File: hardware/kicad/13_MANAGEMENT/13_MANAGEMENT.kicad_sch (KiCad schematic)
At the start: 1 part

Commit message: M3.7: restore native Slice A passive instances
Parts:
- added C_MGMT_VREG_AVDD, C_MGMT_VREG_IN, C_MGMT_VREG_OUT: 4.7uF, symbol RetroSBC-management:C_LOCAL
- added L_MGMT_CORE: 3.3uH, symbol RetroSBC-management:L_LOCAL
- added R_MGMT_VREG_AVDD: 33R, symbol RetroSBC-management:R_LOCAL
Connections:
- net GND: now also C_MGMT_VREG_AVDD.2, C_MGMT_VREG_IN.2, C_MGMT_VREG_OUT.2
- net MGMT_1V1: now also C_MGMT_VREG_OUT.1, L_MGMT_CORE.2
- net MGMT_3V3: now also C_MGMT_VREG_IN.1, R_MGMT_VREG_AVDD.1
- net VREG_AVDD: now also C_MGMT_VREG_AVDD.1, R_MGMT_VREG_AVDD.2
- new net VREG_LX: L_MGMT_CORE.1
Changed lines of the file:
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@@
     ))
   )
+  (symbol (lib_id "RetroSBC-management:L_LOCAL") (at 149.86 80 0) (unit 1)
+    (exclude_from_sim no) (in_bom yes) (on_board yes)
+    (property "Reference" "L_MGMT_CORE" (at 149.86 77.46 0) (effects (font (size 1.27 1.27))))
+    (property "Value" "3.3uH" (at 149.86 82.54 0) (effects (font (size 1.27 1.27))))
+    (property "Footprint" "" (at 149.86 80 0) (effects (font (size 1.27 1.27)) hide))
+    (property "Datasheet" "" (at 149.86 80 0) (effects (font (size 1.27 1.27)) hide))
+    (property "Description" "RetroSBC local passive" (at 149.86 80 0) (effects (font (size 1.27 1.27)) hide))
+    (pin "1")
+    (pin "2")
+    (instances (project "RetroSBC-13-MANAGEMENT" (path "/7a5d3d51-9e2f-4d31-b7cb-9fbd10b8c301/21111111-1111-4111-8111-222222222222" (reference "L_MGMT_CORE") (unit 1))))
+  )
+  (label "VREG_LX" (at 144.78 80 0) (effects (font (size 1.27 1.27)) (justify right bottom)))
+  (label "MGMT_1V1" (at 154.94 80 180) (effects (font (size 1.27 1.27)) (justify right bottom)))
+  (symbol (lib_id "RetroSBC-management:C_LOCAL") (at 149.86 90 0) (unit 1)
+    (exclude_from_sim no) (in_bom yes) (on_board yes)
+    (property "Reference" "C_MGMT_VREG_IN" (at 149.86 87.46 0) (effects (font (size 1.27 1.27))))
+    (property "Value" "4.7uF" (at 149.86 92.54 0) (effects (font (size 1.27 1.27))))
+    (property "Footprint" "" (at 149.86 90 0) (effects (font (size 1.27 1.27)) hide))
+    (property "Datasheet" "" (at 149.86 90 0) (effects (font (size 1.27 1.27)) hide))
+    (property "Description" "RetroSBC local passive" (at 149.86 90 0) (effects (font (size 1.27 1.27)) hide))
+    (pin "1")
+    (pin "2")
+    (instances (project "RetroSBC-13-MANAGEMENT" (path "/7a5d3d51-9e2f-4d31-b7cb-9fbd10b8c301/31111111-1111-4111-8111-333333333333" (reference "C_MGMT_VREG_IN") (unit 1))))
+  )
+  (label "MGMT_3V3" (at 144.78 90 0) (effects (font (size 1.27 1.27)) (justify right bottom)))
+  (label "GND" (at 154.94 90 180) (effects (font (size 1.27 1.27)) (justify right bottom)))
+  (symbol (lib_id "RetroSBC-management:C_LOCAL") (at 149.86 100 0) (unit 1)
+    (exclude_from_sim no) (in_bom yes) (on_board yes)
+    (property "Reference" "C_MGMT_VREG_OUT" (at 149.86 97.46 0) (effects (font (size 1.27 1.27))))
+    (property "Value" "4.7uF" (at 149.86 102.54 0) (effects (font (size 1.27 1.27))))
+    (property "Footprint" "" (at 149.86 100 0) (effects (font (size 1.27 1.27)) hide))
+    (property "Datasheet" "" (at 149.86 100 0) (effects (font (size 1.27 1.27)) hide))
+    (property "Description" "RetroSBC local passive" (at 149.86 100 0) (effects (font (size 1.27 1.27)) hide))
+    (pin "1")
+    (pin "2")
+    (instances (project "RetroSBC-13-MANAGEMENT" (path "/7a5d3d51-9e2f-4d31-b7cb-9fbd10b8c301/41111111-1111-4111-8111-444444444444" (reference "C_MGMT_VREG_OUT") (unit 1))))
+  )
+  (label "MGMT_1V1" (at 144.78 100 0) (effects (font (size 1.27 1.27)) (justify right bottom)))
+  (label "GND" (at 154.94 100 180) (effects (font (size 1.27 1.27)) (justify right bottom)))
+  (symbol (lib_id "RetroSBC-management:R_LOCAL") (at 149.86 110 0) (unit 1)
+    (exclude_from_sim no) (in_bom yes) (on_board yes)
+    (property "Reference" "R_MGMT_VREG_AVDD" (at 149.86 107.46 0) (effects (font (size 1.27 1.27))))
+    (property "Value" "33R" (at 149.86 112.54 0) (effects (font (size 1.27 1.27))))
+    (property "Footprint" "" (at 149.86 110 0) (effects (font (size 1.27 1.27)) hide))
+    (property "Datasheet" "" (at 149.86 110 0) (effects (font (size 1.27 1.27)) hide))
+    (property "Description" "RetroSBC local passive" (at 149.86 110 0) (effects (font (size 1.27 1.27)) hide))
+    (pin "1")
+    (pin "2")
+    (instances (project "RetroSBC-13-MANAGEMENT" (path "/7a5d3d51-9e2f-4d31-b7cb-9fbd10b8c301/51111111-1111-4111-8111-555555555555" (reference "R_MGMT_VREG_AVDD") (unit 1))))
+  )
+  (label "MGMT_3V3" (at 144.78 110 0) (effects (font (size 1.27 1.27)) (justify right bottom)))
+  (label "VREG_AVDD" (at 154.94 110 180) (effects (font (size 1.27 1.27)) (justify right bottom)))
+  (symbol (lib_id "RetroSBC-management:C_LOCAL") (at 149.86 120 0) (unit 1)
+    (exclude_from_sim no) (in_bom yes) (on_board yes)
+    (property "Reference" "C_MGMT_VREG_AVDD" (at 149.86 117.46 0) (effects (font (size 1.27 1.27))))
+    (property "Value" "4.7uF" (at 149.86 122.54 0) (effects (font (size 1.27 1.27))))
+    (property "Footprint" "" (at 149.86 120 0) (effects (font (size 1.27 1.27)) hide))
+    (property "Datasheet" "" (at 149.86 120 0) (effects (font (size 1.27 1.27)) hide))
+    (property "Description" "RetroSBC local passive" (at 149.86 120 0) (effects (font (size 1.27 1.27)) hide))
+    (pin "1")
+    (pin "2")
+    (instances (project "RetroSBC-13-MANAGEMENT" (path "/7a5d3d51-9e2f-4d31-b7cb-9fbd10b8c301/61111111-1111-4111-8111-666666666666" (reference "C_MGMT_VREG_AVDD") (unit 1))))
+  )
+  (label "VREG_AVDD" (at 144.78 120 0) (effects (font (size 1.27 1.27)) (justify right bottom)))
+  (label "GND" (at 154.94 120 180) (effects (font (size 1.27 1.27)) (justify right bottom)))
+  (label "MGMT_3V3" (at 69.52000000000001 113.97 0)
+    (effects (font (size 1.27 1.27)) (justify left bottom))
+)
+  (label "MGMT_1V1" (at 69.52000000000001 101.27 0)
+    (effects (font (size 1.27 1.27)) (justify left bottom))
+)
+  (label "MGMT_3V3" (at 69.52000000000001 88.57 0)
+    (effects (font (size 1.27 1.27)) (justify left bottom))
+)
+  (label "MGMT_3V3" (at 87.03999999999999 74.6 90)
+    (effects (font (size 1.27 1.27)) (justify left bottom))
+)
+  (label "MGMT_3V3" (at 97.19 74.6 90)
+    (effects (font (size 1.27 1.27)) (justify left bottom))
+)
+  (label "MGMT_1V1" (at 103.28 74.6 90)
+    (effects (font (size 1.27 1.27)) (justify left bottom))
+)
+  (label "MGMT_3V3" (at 130.48 75.87 180)
+    (effects (font (size 1.27 1.27)) (justify left bottom))
+)
+  (label "MGMT_3V3" (at 130.48 98.73 180)
+    (effects (font (size 1.27 1.27)) (justify left bottom))
+)
+  (label "MGMT_1V1" (at 130.48 101.27 180)
+    (effects (font (size 1.27 1.27)) (justify left bottom))
+)
+  (label "MGMT_3V3" (at 130.48 121.59 180)
+    (effects (font (size 1.27 1.27)) (justify left bottom))
+)
+  (label "MGMT_3V3" (at 130.48 124.13 180)
+    (effects (font (size 1.27 1.27)) (justify left bottom))
+)
+  (label "MGMT_3V3" (at 104.84 125.4 270)
+    (effects (font (size 1.27 1.27)) (justify left bottom))
+)
+  (label "MGMT_3V3" (at 102.81 125.4 270)
+    (effects (font (size 1.27 1.27)) (justify left bottom))
+)
+  (label "MGMT_3V3" (at 88.60000000000001 125.4 270)
+    (effects (font (size 1.27 1.27)) (justify left bottom))
+)
   (label "VREG_AVDD" (at 119.05 69.52 90)
     (effects (font (size 1.27 1.27)) (justify left bottom))

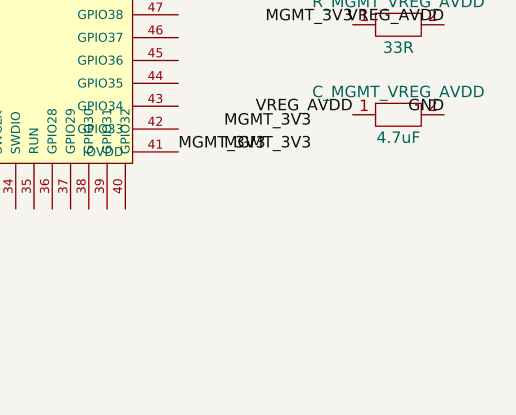
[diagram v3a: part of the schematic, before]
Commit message: M3.7: materialize locked management bulk and rail decoupling
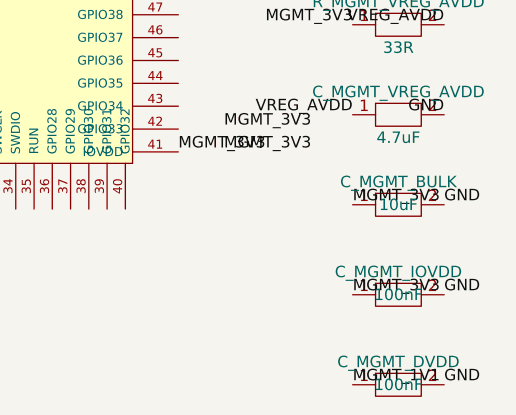
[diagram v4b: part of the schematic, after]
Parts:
- added C_MGMT_BULK: 10uF, symbol RetroSBC-management:C_LOCAL
- added C_MGMT_DVDD, C_MGMT_IOVDD: 100nF, symbol RetroSBC-management:C_LOCAL
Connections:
- net GND: now also C_MGMT_BULK.2, C_MGMT_DVDD.2, C_MGMT_IOVDD.2
- net MGMT_1V1: now also C_MGMT_DVDD.1
- net MGMT_3V3: now also C_MGMT_BULK.1, C_MGMT_IOVDD.1
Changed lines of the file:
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@@
+    (effects (font (size 1.27 1.27)) (justify left bottom))
+)
+  (symbol (lib_id "RetroSBC-management:C_LOCAL") (at 149.86 130 0) (unit 1)
+    (exclude_from_sim no) (in_bom yes) (on_board yes)
+    (property "Reference" "C_MGMT_BULK" (at 149.86 127.46 0) (effects (font (size 1.27 1.27))))
+    (property "Value" "10uF" (at 149.86 130 0) (effects (font (size 1.27 1.27))))
+    (property "Footprint" "" (at 149.86 130 0) (effects (font (size 1.27 1.27)) hide))
+    (property "Datasheet" "" (at 149.86 130 0) (effects (font (size 1.27 1.27)) hide))
+    (property "Description" "RetroSBC local passive" (at 149.86 130 0) (effects (font (size 1.27 1.27)) hide))
+    (pin "1")
+    (pin "2")
+    (instances (project "RetroSBC-13-MANAGEMENT"
+      (path "/7a5d3d51-9e2f-4d31-b7cb-9fbd10b8c301/c0000101-6666-4666-8666-000000000101" (reference "C_MGMT_BULK") (unit 1))
+    ))
+  )
+  (label "MGMT_3V3" (at 144.78 130 0)
+    (effects (font (size 1.27 1.27)) (justify left bottom))
+)
+  (label "GND" (at 154.94 130 180)
+    (effects (font (size 1.27 1.27)) (justify left bottom))
+)
+  (symbol (lib_id "RetroSBC-management:C_LOCAL") (at 149.86 140 0) (unit 1)
+    (exclude_from_sim no) (in_bom yes) (on_board yes)
+    (property "Reference" "C_MGMT_IOVDD" (at 149.86 137.46 0) (effects (font (size 1.27 1.27))))
+    (property "Value" "100nF" (at 149.86 140 0) (effects (font (size 1.27 1.27))))
+    (property "Footprint" "" (at 149.86 140 0) (effects (font (size 1.27 1.27)) hide))
+    (property "Datasheet" "" (at 149.86 140 0) (effects (font (size 1.27 1.27)) hide))
+    (property "Description" "RetroSBC local passive" (at 149.86 140 0) (effects (font (size 1.27 1.27)) hide))
+    (pin "1")
+    (pin "2")
+    (instances (project "RetroSBC-13-MANAGEMENT"
+      (path "/7a5d3d51-9e2f-4d31-b7cb-9fbd10b8c301/c0000102-6666-4666-8666-000000000102" (reference "C_MGMT_IOVDD") (unit 1))
+    ))
+  )
+  (label "MGMT_3V3" (at 144.78 140 0)
+    (effects (font (size 1.27 1.27)) (justify left bottom))
+)
+  (label "GND" (at 154.94 140 180)
+    (effects (font (size 1.27 1.27)) (justify left bottom))
+)
+  (symbol (lib_id "RetroSBC-management:C_LOCAL") (at 149.86 150 0) (unit 1)
+    (exclude_from_sim no) (in_bom yes) (on_board yes)
+    (property "Reference" "C_MGMT_DVDD" (at 149.86 147.46 0) (effects (font (size 1.27 1.27))))
+    (property "Value" "100nF" (at 149.86 150 0) (effects (font (size 1.27 1.27))))
+    (property "Footprint" "" (at 149.86 150 0) (effects (font (size 1.27 1.27)) hide))
+    (property "Datasheet" "" (at 149.86 150 0) (effects (font (size 1.27 1.27)) hide))
+    (property "Description" "RetroSBC local passive" (at 149.86 150 0) (effects (font (size 1.27 1.27)) hide))
+    (pin "1")
+    (pin "2")
+    (instances (project "RetroSBC-13-MANAGEMENT"
+      (path "/7a5d3d51-9e2f-4d31-b7cb-9fbd10b8c301/c0000103-6666-4666-8666-000000000103" (reference "C_MGMT_DVDD") (unit 1))
+    ))
+  )
+  (label "MGMT_1V1" (at 144.78 150 0)
+    (effects (font (size 1.27 1.27)) (justify left bottom))
+)
+  (label "GND" (at 154.94 150 180)
     (effects (font (size 1.27 1.27)) (justify left bottom))
 )

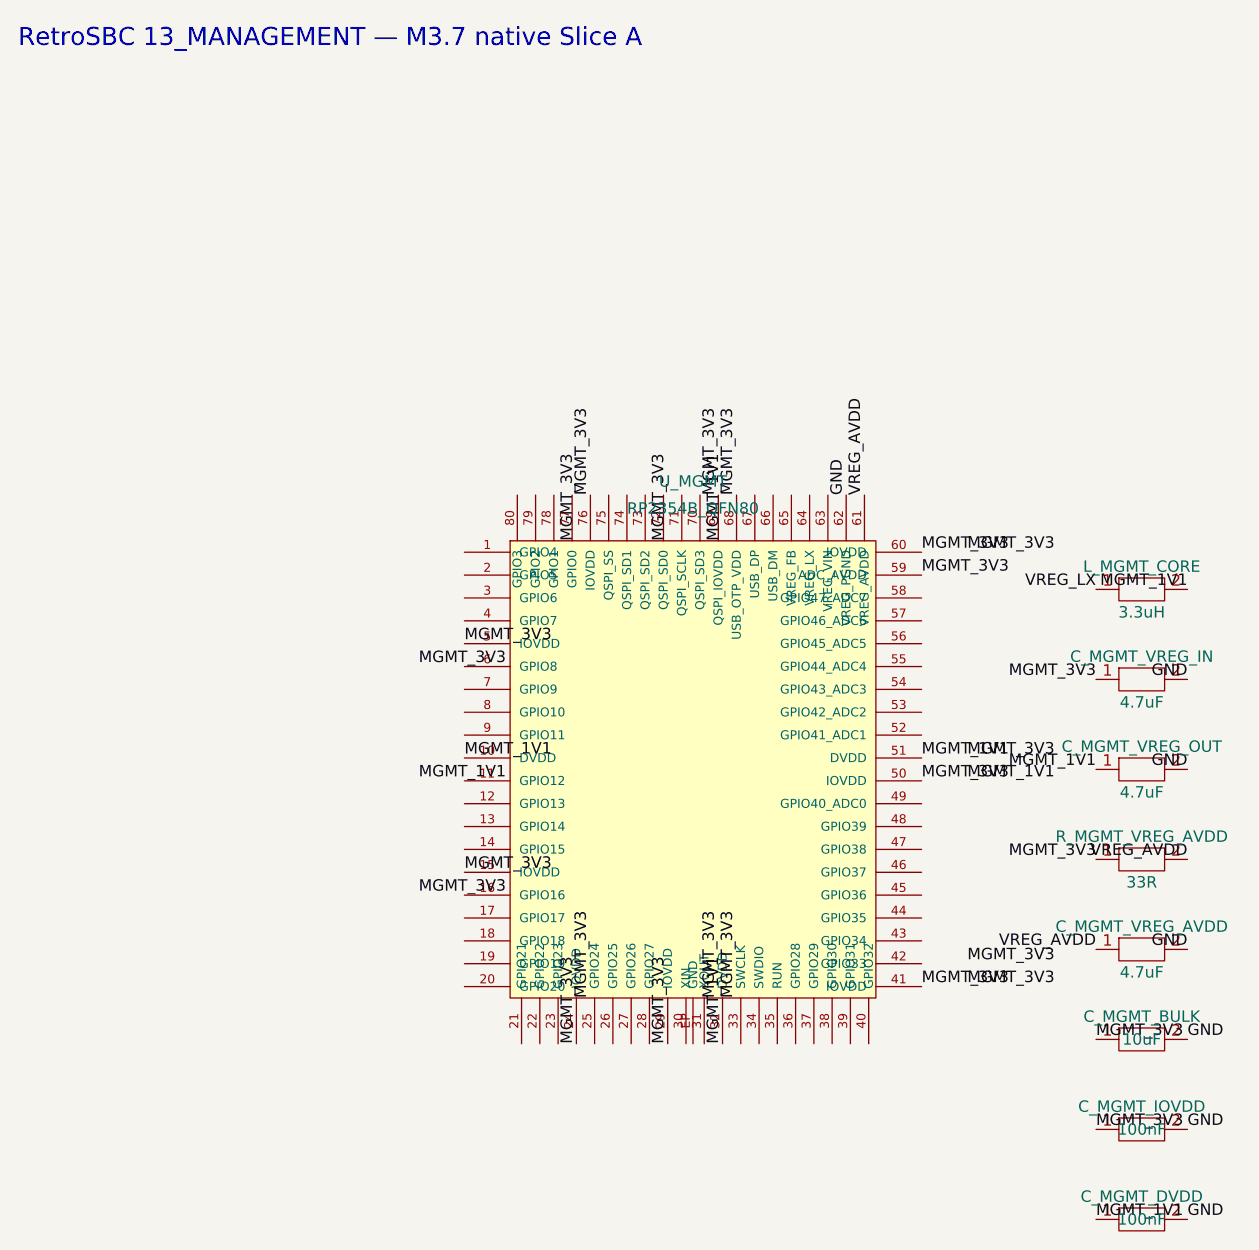
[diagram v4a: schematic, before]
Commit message: M3.7: remove stale Slice B labels and restore regulator endpoint nets
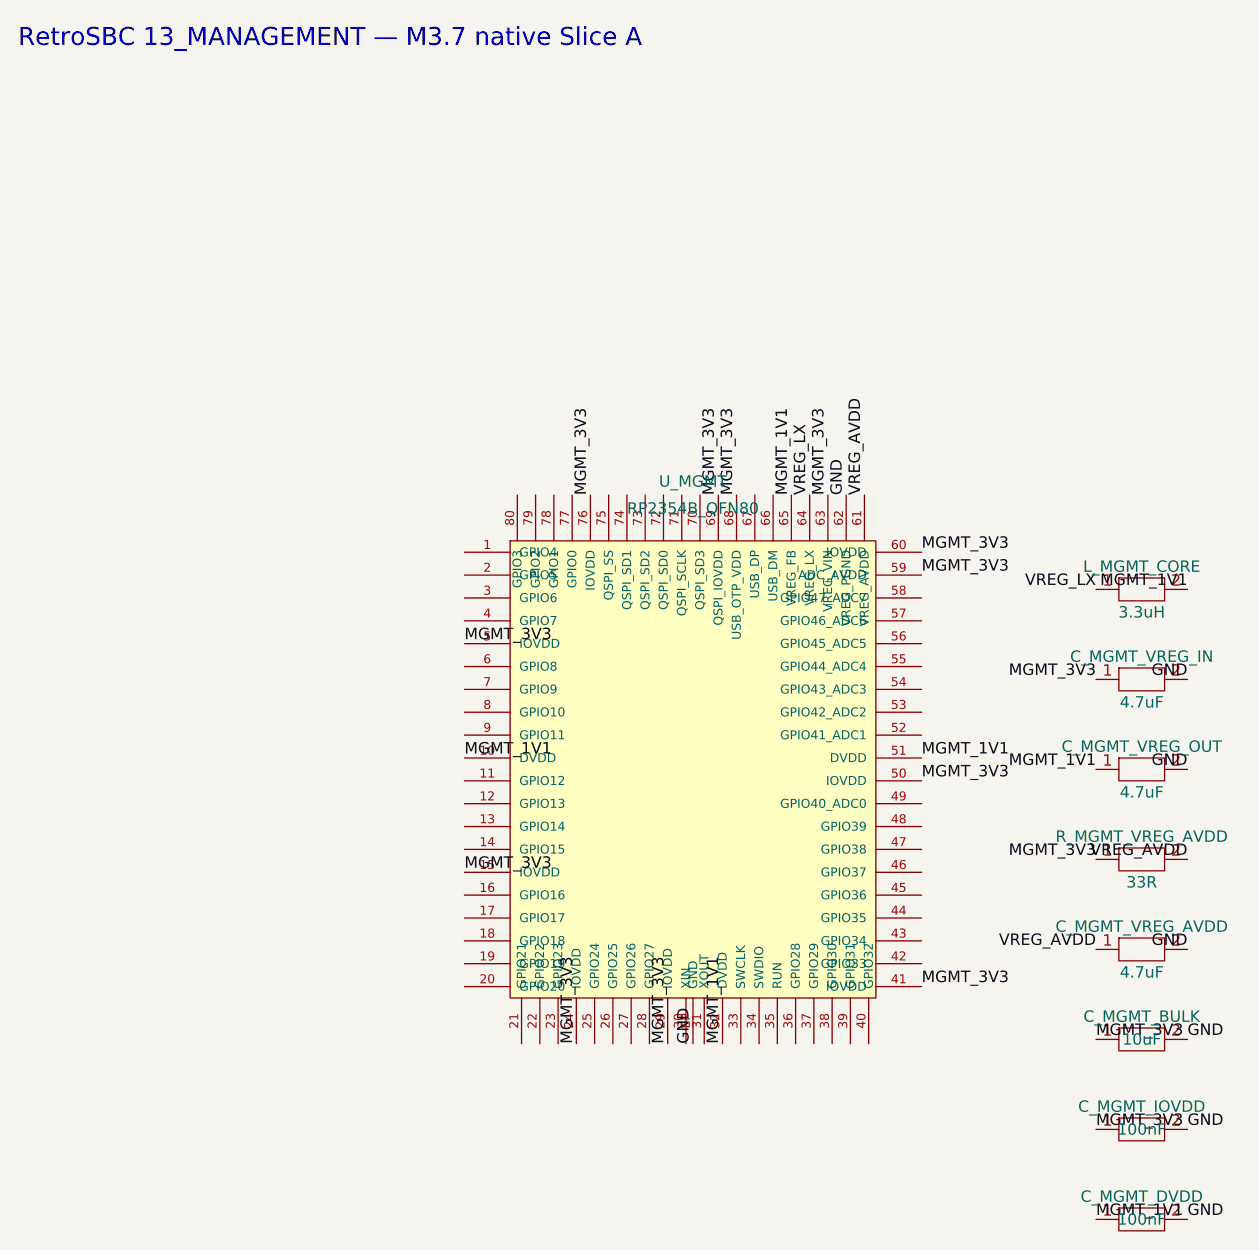
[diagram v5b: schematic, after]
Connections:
- net GND: now also U_MGMT.EP (GND)
- net MGMT_1V1: now also U_MGMT.65 (VREG_FB)
- net MGMT_3V3: now also U_MGMT.63 (VREG_VIN)
- net VREG_LX: now also U_MGMT.64 (VREG_LX)
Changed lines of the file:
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@@
   (label "VREG_AVDD" (at 144.78 120 0) (effects (font (size 1.27 1.27)) (justify right bottom)))
   (label "GND" (at 154.94 120 180) (effects (font (size 1.27 1.27)) (justify right bottom)))
-  (label "MGMT_3V3" (at 69.52000000000001 113.97 0)
-    (effects (font (size 1.27 1.27)) (justify left bottom))
-)
-  (label "MGMT_1V1" (at 69.52000000000001 101.27 0)
-    (effects (font (size 1.27 1.27)) (justify left bottom))
-)
-  (label "MGMT_3V3" (at 69.52000000000001 88.57 0)
-    (effects (font (size 1.27 1.27)) (justify left bottom))
-)
-  (label "MGMT_3V3" (at 87.03999999999999 74.6 90)
-    (effects (font (size 1.27 1.27)) (justify left bottom))
-)
-  (label "MGMT_3V3" (at 97.19 74.6 90)
-    (effects (font (size 1.27 1.27)) (justify left bottom))
-)
-  (label "MGMT_1V1" (at 103.28 74.6 90)
-    (effects (font (size 1.27 1.27)) (justify left bottom))
-)
-  (label "MGMT_3V3" (at 130.48 75.87 180)
-    (effects (font (size 1.27 1.27)) (justify left bottom))
-)
-  (label "MGMT_3V3" (at 130.48 98.73 180)
-    (effects (font (size 1.27 1.27)) (justify left bottom))
-)
-  (label "MGMT_1V1" (at 130.48 101.27 180)
-    (effects (font (size 1.27 1.27)) (justify left bottom))
-)
-  (label "MGMT_3V3" (at 130.48 121.59 180)
-    (effects (font (size 1.27 1.27)) (justify left bottom))
-)
-  (label "MGMT_3V3" (at 130.48 124.13 180)
-    (effects (font (size 1.27 1.27)) (justify left bottom))
-)
-  (label "MGMT_3V3" (at 104.84 125.4 270)
-    (effects (font (size 1.27 1.27)) (justify left bottom))
-)
-  (label "MGMT_3V3" (at 102.81 125.4 270)
-    (effects (font (size 1.27 1.27)) (justify left bottom))
-)
-  (label "MGMT_3V3" (at 88.60000000000001 125.4 270)
-    (effects (font (size 1.27 1.27)) (justify left bottom))
-)
   (label "VREG_AVDD" (at 119.05 69.52 90)
     (effects (font (size 1.27 1.27)) (justify left bottom))
@@
     (effects (font (size 1.27 1.27)) (justify left bottom))
 )
+  (label "MGMT_3V3" (at 114.99 69.52 90)
+    (effects (font (size 1.27 1.27)) (justify left bottom))
+)
+  (label "VREG_LX" (at 112.96 69.52 90)
+    (effects (font (size 1.27 1.27)) (justify left bottom))
+)
+  (label "MGMT_1V1" (at 110.93 69.52 90)
+    (effects (font (size 1.27 1.27)) (justify left bottom))
+)
+  (label "GND" (at 100 130.48 270)
+    (effects (font (size 1.27 1.27)) (justify left bottom))
+)
